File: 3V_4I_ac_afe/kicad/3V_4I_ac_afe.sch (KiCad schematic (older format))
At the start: 4 parts

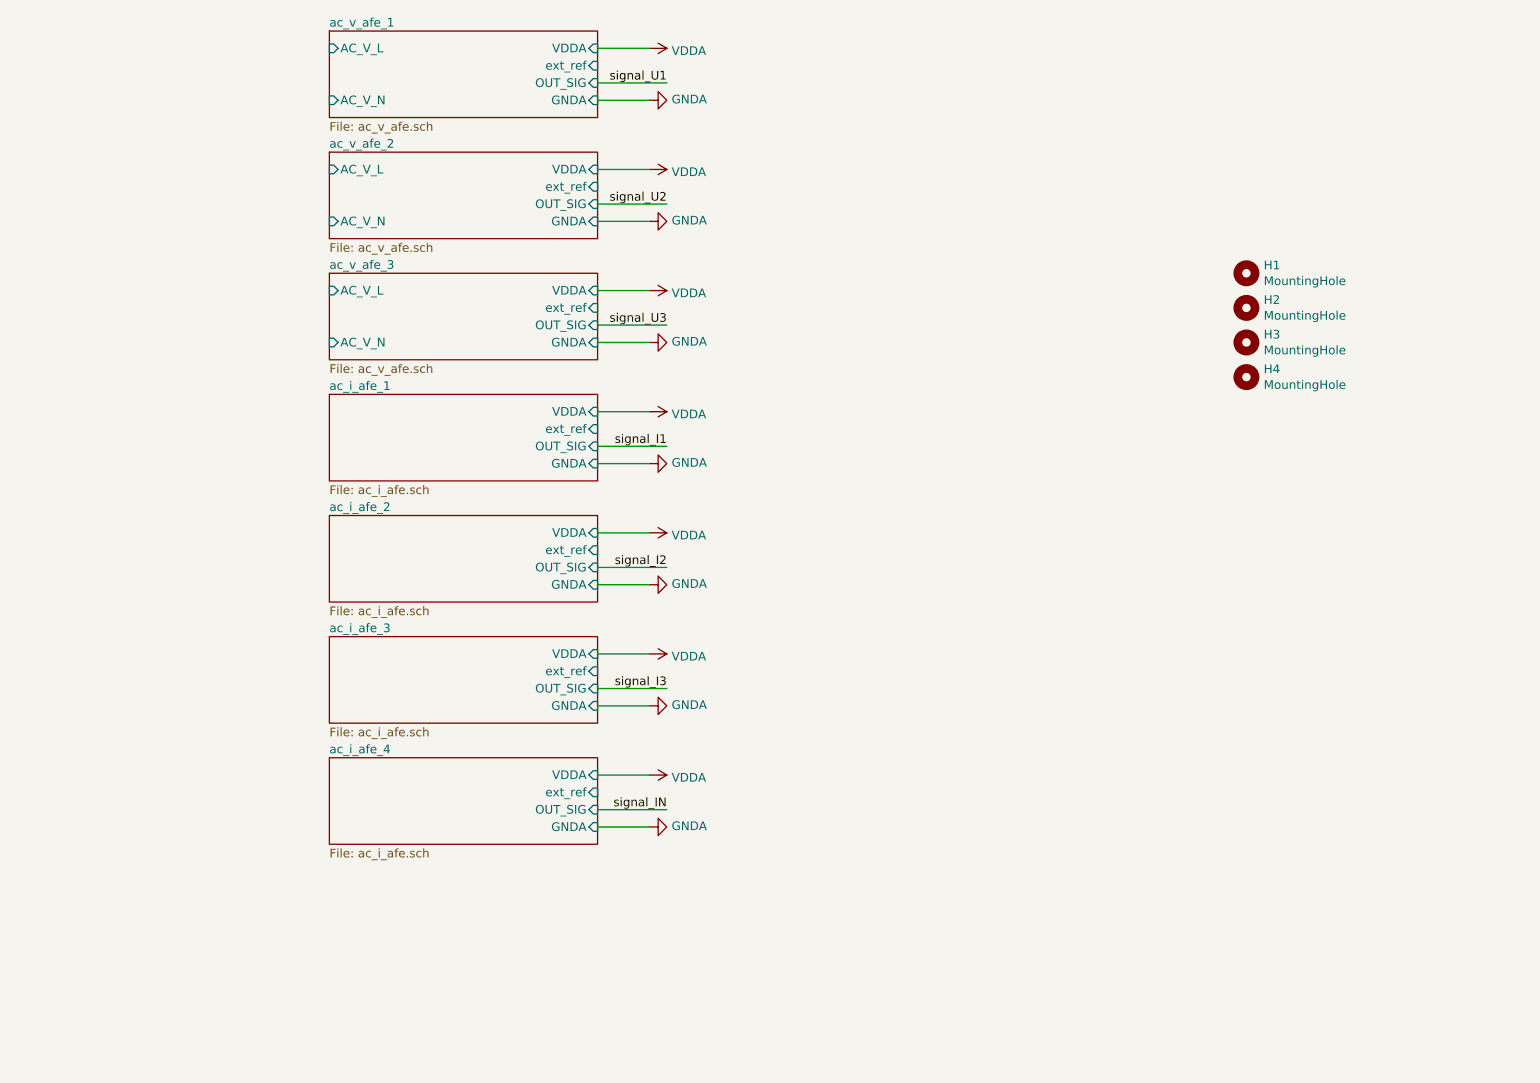
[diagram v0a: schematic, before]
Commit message: added few prototypes and script for zipping kicad gerbers
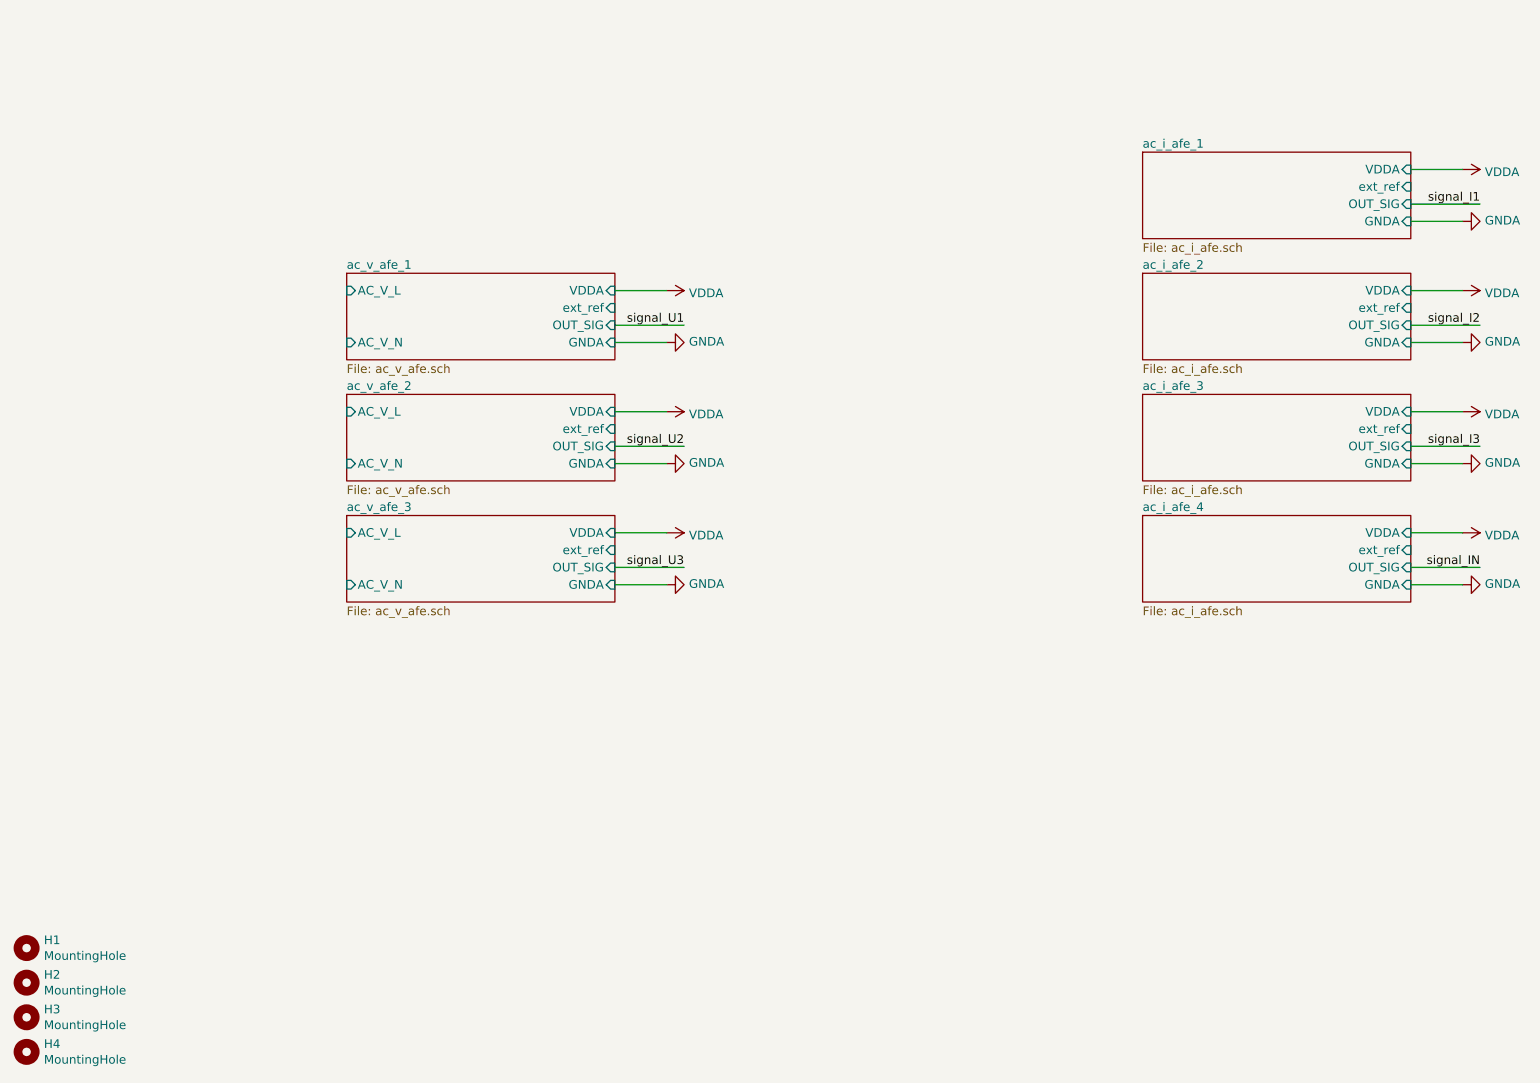
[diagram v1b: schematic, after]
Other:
- moved on the sheet: H1, H2, H3, H4
